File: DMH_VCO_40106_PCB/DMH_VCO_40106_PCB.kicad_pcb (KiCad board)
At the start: 2 copper layers, 98 x 135 mm, 147 parts, among them J10 Panel_GND, J100 IDC_02x08, J150 Conn_01x12, J300 AVR-ISP-6, Q1 BC558, Q2 BC548, Q3 BC548, Q4 BC548, Q5 BC548, Q6 BC548, Q7 J113, SW1 SW_SPDT_321_OnOff, SW2 SW_SPDT_321_OnOff, SW3 SW_SPDT_321_OnOff, U1 40106, U2 TL074, U3 TL074, U4 TL074, U5 ATtiny4313-P, U6 SM420561N

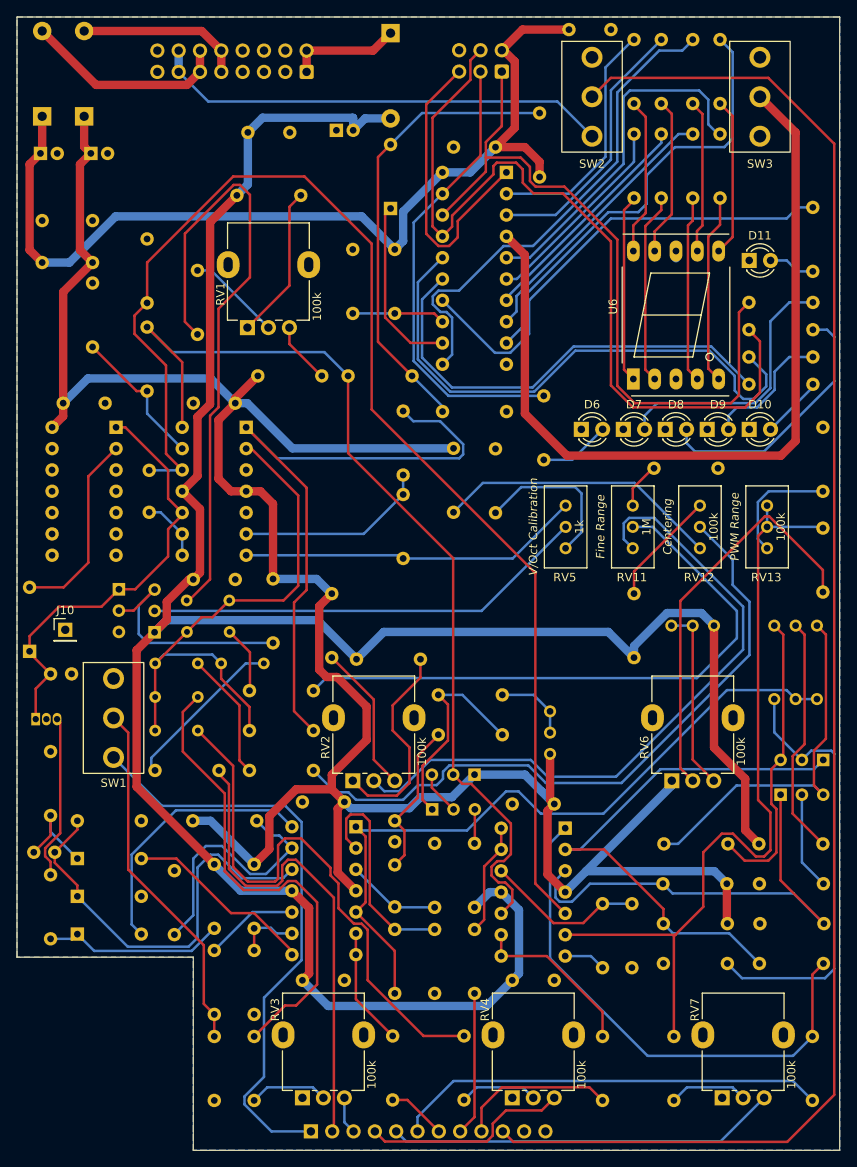
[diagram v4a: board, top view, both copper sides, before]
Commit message: Updated PCB with rerouting of square wave to tuner
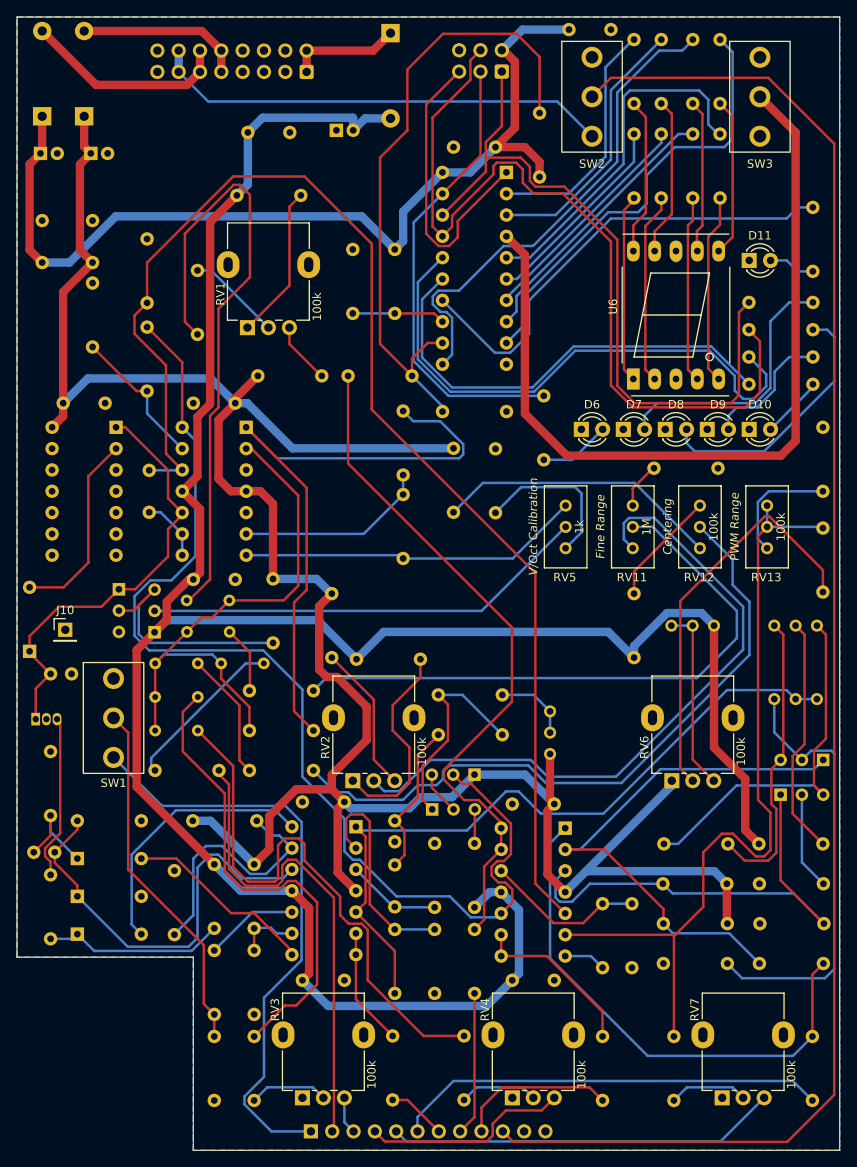
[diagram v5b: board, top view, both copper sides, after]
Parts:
- removed D5: 1N4148, Diode_THT:D_DO-35_SOD27_P7.62mm_Horizontal
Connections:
- R21 pad 1: Net-(U4D--) -> /Core/Square
- R54 pad 1: /Core/Sawtooth -> /Core/Square
- R54 pad 2: Net-(D5-A) -> Net-(U5-PB0)
- R56 pad 1: Net-(D5-A) -> Net-(U5-PB0)
- R57 pad 2: Net-(D5-A) -> Net-(U5-PB0)
- U4 pad 13: Net-(U4D--) -> /Core/Square
- U4 pad 14: Net-(U4D--) -> /Core/Square
- U5 pad 12: Net-(D5-K) -> Net-(U5-PB0)
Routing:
- net /Core/Square: track 0.00 -> 82.5 mm
- net Net-(U5-PB0): track 0.00 -> 77.0 mm
- net Net-(D5-A): track 54.9 -> 0.00 mm
- net Net-(D5-K): track 21.3 -> 0.00 mm
- net /Core/Sawtooth: track 116.2 -> 133.2 mm
- net Net-(U4D--): track 13.4 -> 0.00 mm

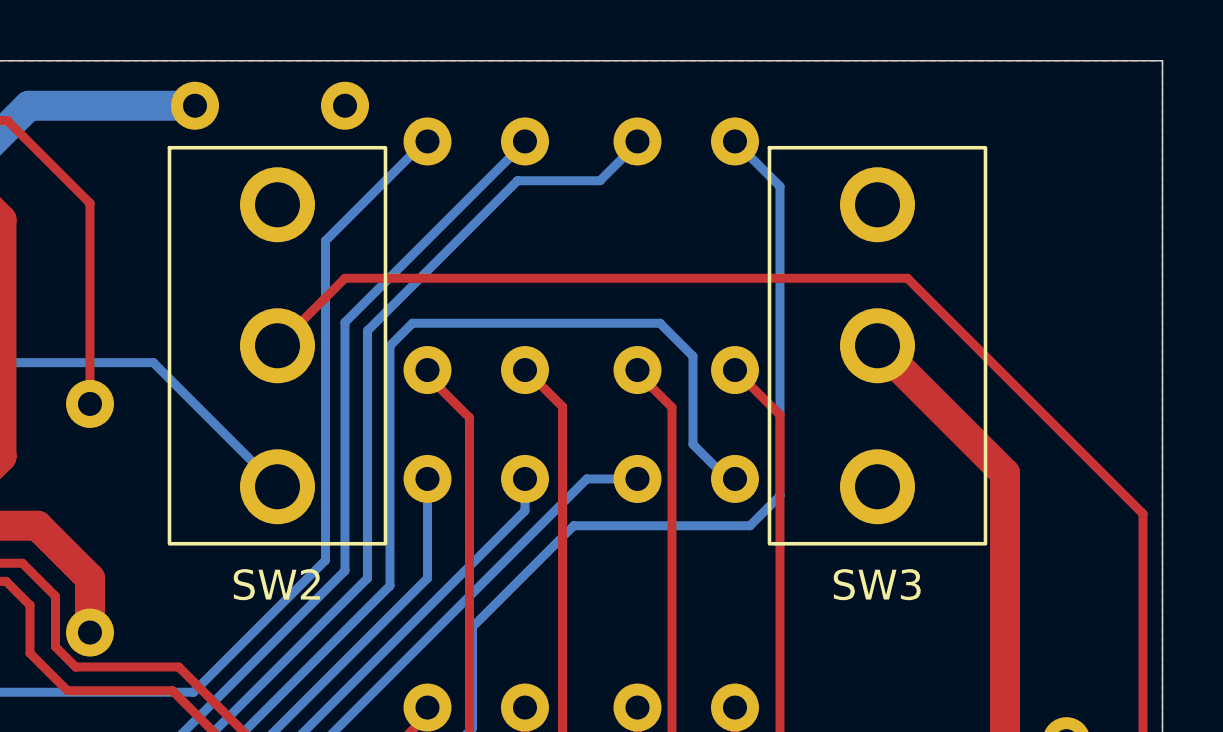
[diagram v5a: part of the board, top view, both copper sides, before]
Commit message: Added pull up resistor to tuner switch
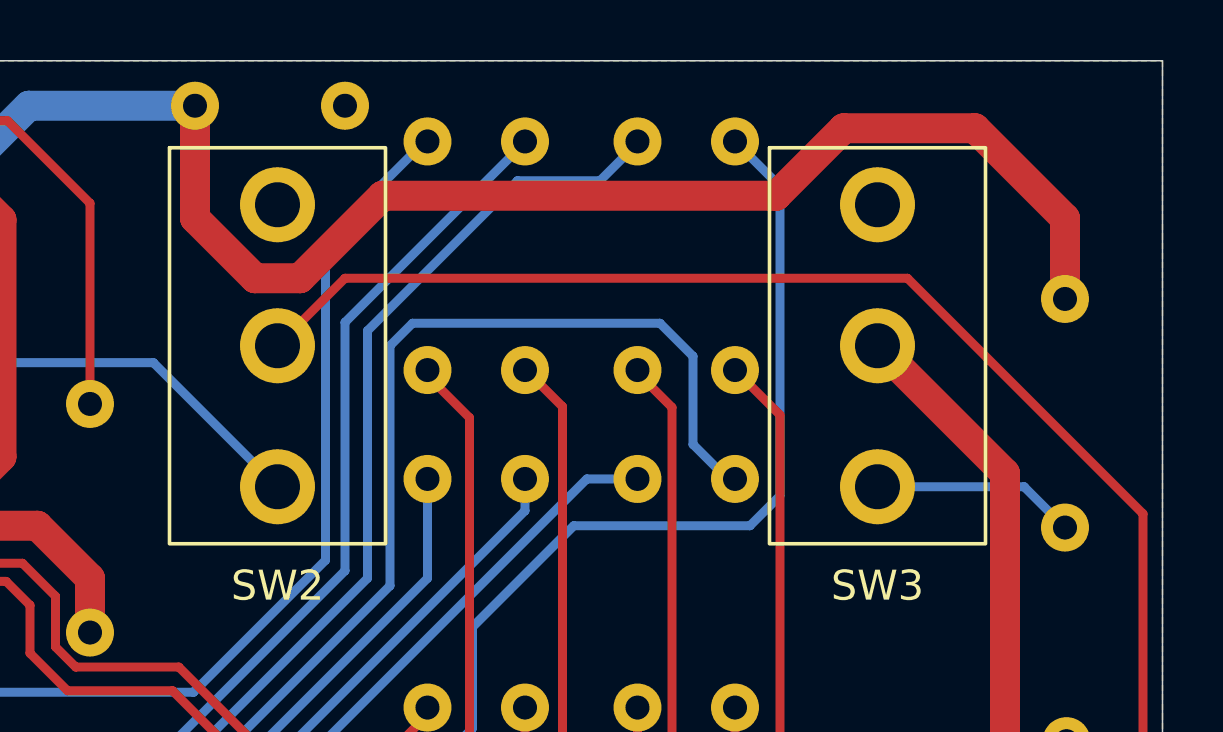
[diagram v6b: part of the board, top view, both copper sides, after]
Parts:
- added R74: 100k, Resistor_THT:R_Axial_DIN0207_L6.3mm_D2.5mm_P7.62mm_Horizontal, B.Cu at (145.8, 70.4)
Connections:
- SW3 pad 1: unconnected-(SW3-C-Pad1) -> Net-(SW3-C)
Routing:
- net +5V: track 113.7 -> 153.3 mm
- net Net-(SW3-C): track 0.00 -> 6.81 mm
